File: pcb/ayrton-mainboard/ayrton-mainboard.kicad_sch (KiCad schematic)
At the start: 0 parts

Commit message: Continued initial system design
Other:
- sheet PCIe and 10 SFP+ renamed PCIe and 10G SFP+
- added sheet ADC interfaces (adc-interfaces.kicad_sch)
- added sheet PLL (pll.kicad_sch)
- added sheet Power Supply (psu.kicad_sch)
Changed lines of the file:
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@@
 	(title_block
 		(title "AYRTON Main Board")
-		(date "2024-11-15")
+		(date "2024-11-18")
 		(rev "0.1")
 		(company "Antikernel Labs")
@@
 	)
 	(sheet
+		(at 45.72 99.06)
+		(size 29.21 44.45)
+		(fields_autoplaced yes)
+		(stroke
+			(width 0.1524)
+			(type solid)
+		)
+		(fill
+			(color 0 0 0 0.0000)
+		)
+		(property "Sheetname" "Power Supply"
+			(at 45.72 98.3484 0)
+			(effects
+				(font
+					(size 1.27 1.27)
+				)
+				(justify left bottom)
+			)
+		)
+		(property "Sheetfile" "psu.kicad_sch"
+			(at 45.72 144.0946 0)
+			(effects
+				(font
+					(size 1.27 1.27)
+				)
+				(justify left top)
+			)
+		)
+		(instances
+			(project "ayrton-mainboard"
+				(path "/11b16c18-86a9-45f7-bd03-4e81057d99ff"
+					(page "9")
+				)
+			)
+		)
+	)
+	(sheet
+		(at 175.895 103.505)
+		(size 34.925 41.275)
+		(fields_autoplaced yes)
+		(stroke
+			(width 0.1524)
+			(type solid)
+		)
+		(fill
+			(color 0 0 0 0.0000)
+		)
+		(property "Sheetname" "PLL"
+			(at 175.895 102.7934 0)
+			(effects
+				(font
+					(size 1.27 1.27)
+				)
+				(justify left bottom)
+			)
+		)
+		(property "Sheetfile" "pll.kicad_sch"
+			(at 175.895 145.3646 0)
+			(effects
+				(font
+					(size 1.27 1.27)
+				)
+				(justify left top)
+			)
+		)
+		(instances
+			(project "ayrton-mainboard"
+				(path "/11b16c18-86a9-45f7-bd03-4e81057d99ff"
+					(page "12")
+				)
+			)
+		)
+	)
+	(sheet
 		(at 176.53 26.67)
 		(size 30.48 36.83)
@@
 			(color 0 0 0 0.0000)
 		)
-		(property "Sheetname" "PCIe and 10 SFP+"
+		(property "Sheetname" "PCIe and 10G SFP+"
 			(at 176.53 25.9584 0)
 			(effects
@@
 				)
 			)
+		)
+	)
+	(sheet
+		(at 104.14 101.6)
+		(size 40.64 44.45)
+		(fields_autoplaced yes)
+		(stroke
+			(width 0.1524)
+			(type solid)
+		)
+		(fill
+			(color 0 0 0 0.0000)
+		)
+		(property "Sheetname" "ADC interfaces"
+			(at 104.14 100.8884 0)
+			(effects
+				(font
+					(size 1.27 1.27)
+				)
+				(justify left bottom)
+			)
+		)
+		(property "Sheetfile" "adc-interfaces.kicad_sch"
+			(at 104.14 146.6346 0)
+			(effects
+				(font
+					(size 1.27 1.27)
+				)
+				(justify left top)
+			)
+		)
+		(instances
+			(project "ayrton-mainboard"
+				(path "/11b16c18-86a9-45f7-bd03-4e81057d99ff"
+					(page "11")
+				)
+			)

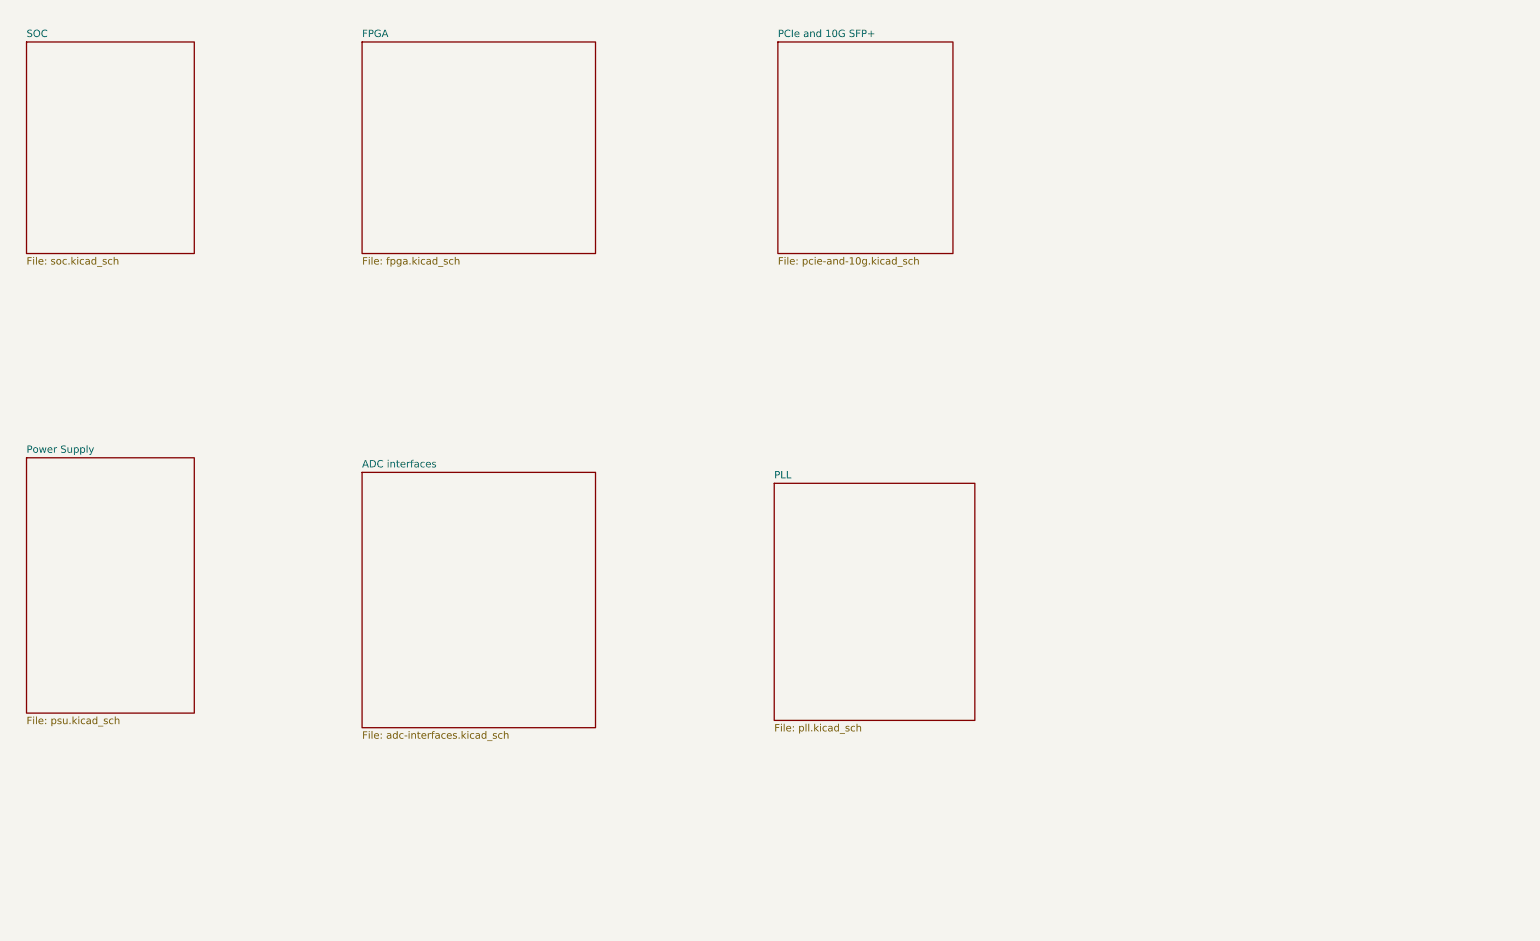
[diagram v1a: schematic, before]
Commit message: Continued initial schematic, working on LPDDR4
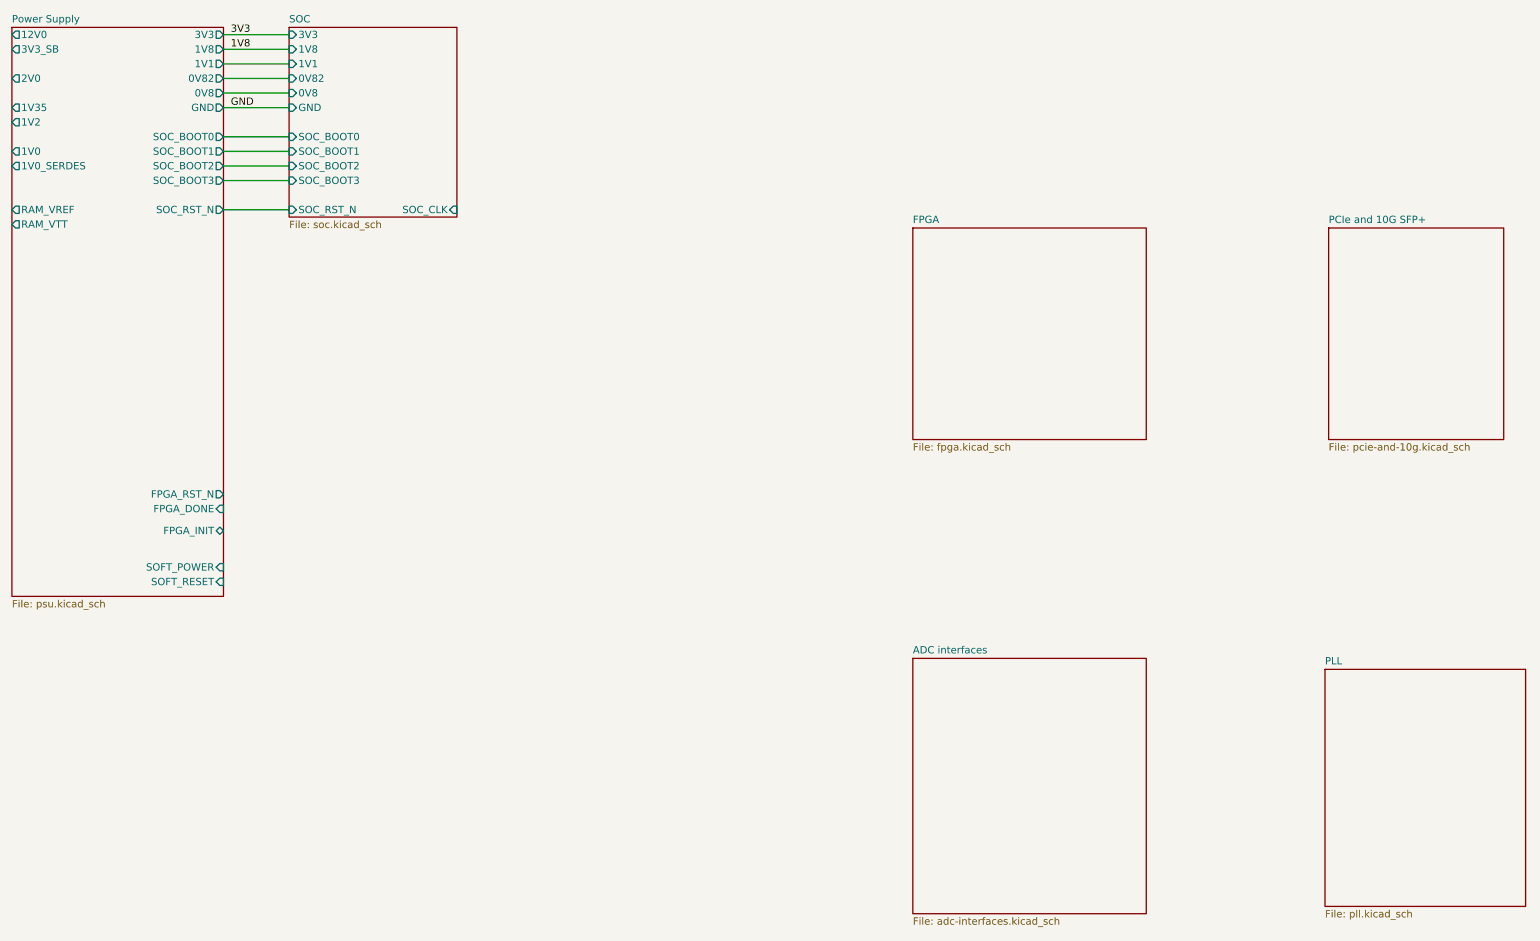
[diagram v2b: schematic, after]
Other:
- sheet Power Supply ports: added 0V8, 0V82, 12V0, 1V0, 1V0_SERDES, 1V1, 1V2, 1V35, 1V8, 2V0, 3V3, 3V3_SB, FPGA_DONE, FPGA_INIT, FPGA_RST_N, GND, RAM_VREF, RAM_VTT, SOC_BOOT0, SOC_BOOT1, SOC_BOOT2, SOC_BOOT3, SOC_RST_N, SOFT_POWER, SOFT_RESET; removed none
- sheet SOC ports: added 0V8, 0V82, 1V1, 1V8, 3V3, GND, SOC_BOOT0, SOC_BOOT1, SOC_BOOT2, SOC_BOOT3, SOC_CLK, SOC_RST_N; removed none
